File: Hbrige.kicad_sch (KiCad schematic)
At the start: 15 parts, among them U4 CSD88537ND, U5 CSD88537ND

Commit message: reintroduction des mosfet (au lieu des demi-ponts en H), début routage
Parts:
- removed U4, U5: CSD88537ND, CSD88537ND:SOIC127P599X175-8N, symbol CSD88537ND:CSD88537ND
- added J4: Conn_01x02, KF301-5.0-2P:KF301-5.0-2P, symbol Connector_Generic:Conn_01x02
- added U4, U5, U6, U7: ~, TPH1R403NL:TPH1R403NL, symbol DRV8701:TPH1R403NL
- C10, C8: value 0.1u -> 100n; footprint Capacitor_SMD:C_0603_1608Metric_Pad1.08x0.95mm_HandSolder -> Capacitor_SMD:C_0402_1005Metric
- C6, C7, C9: footprint Capacitor_SMD:C_0603_1608Metric_Pad1.08x0.95mm_HandSolder -> Capacitor_SMD:C_0402_1005Metric
- R10, R11, R6, R7, R8, R9: footprint Resistor_SMD:R_0402_1005Metric_Pad0.72x0.64mm_HandSolder -> Resistor_SMD:R_0402_1005Metric
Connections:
- net SH1: now also U3.18 (SH1), J4.2 (Pin_2), U6.5 (D), U6.6 (D), U6.7 (D), U6.8 (D), U6.9 (D), U7.1 (S), U7.2 (S), U7.3 (S)
- net SH2: now also J4.1 (Pin_1), U4.1 (S), U4.2 (S), U4.3 (S), U5.5 (D), U5.6 (D), U5.7 (D), U5.8 (D), U5.9 (D)
- net VDC: now also U4.5 (D), U4.6 (D), U4.7 (D), U4.8 (D), U4.9 (D), U7.5 (D), U7.6 (D), U7.7 (D), U7.8 (D), U7.9 (D)
- net at U3.17 (GH1): now also U7.4 (G)
- net at U3.19 (GL1): now also U6.4 (G)
- net SP: now reaches R11.1, U3.21 (SP)
- net SP: now also U5.1 (S), U5.2 (S), U5.3 (S), U6.1 (S), U6.2 (S), U6.3 (S)
- net at U3.22 (GL2): now also U5.4 (G)
- net at U3.24 (GH2): now also U4.4 (G)

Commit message: maj PCB
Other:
- moved on the sheet: J4
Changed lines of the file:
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@@
 	(wire
 		(pts
-			(xy 217.17 83.82) (xy 217.17 102.87)
+			(xy 217.17 87.63) (xy 217.17 102.87)
 		)
 		(stroke
@@
 	(wire
 		(pts
-			(xy 217.17 81.28) (xy 217.17 69.85)
+			(xy 217.17 85.09) (xy 217.17 69.85)
 		)
 		(stroke
@@
 	(symbol
 		(lib_id "Connector_Generic:Conn_01x02")
-		(at 222.25 81.28 0)
+		(at 222.25 85.09 0)
 		(unit 1)
 		(exclude_from_sim no)
@@
 		(dnp no)
 		(property "Reference" "J4"
-			(at 221.996 89.408 90)
+			(at 221.996 93.218 90)
 			(effects
 				(font
@@
 		)
 		(property "Value" "Conn_01x02"
-			(at 224.79 87.884 90)
+			(at 224.79 91.694 90)
 			(effects
 				(font
@@
 		)
 		(property "Footprint" "KF301-5.0-2P:KF301-5.0-2P"
-			(at 222.25 81.28 0)
+			(at 222.25 85.09 0)
 			(effects
 				(font
@@
 		)
 		(property "Datasheet" "~"
-			(at 222.25 81.28 0)
+			(at 222.25 85.09 0)
 			(effects
 				(font
@@
 		)
 		(property "Description" "Generic connector, single row, 01x02, script generated (kicad-library-utils/schlib/autogen/connector/)"
-			(at 222.25 81.28 0)
-			(effects
-				(font
+			(at 222.25 85.09 0)
+			(effects
+				(font

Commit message: finalisation PCB
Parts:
- removed C6: 1u, Capacitor_SMD:C_0402_1005Metric, symbol Device:C
- removed R10: 3.3k, Resistor_SMD:R_0402_1005Metric, symbol Device:R
- removed R11: 50m, Resistor_SMD:R_0402_1005Metric, symbol Device:R
- removed R6, R7: 10k, Resistor_SMD:R_0402_1005Metric, symbol Device:R
- removed R8: 33k, Resistor_SMD:R_0402_1005Metric, symbol Device:R
- removed R9: 2k, Resistor_SMD:R_0402_1005Metric, symbol Device:R
- added C12: 1u, Capacitor_SMD:C_0402_1005Metric, symbol Device:C
- renumbered C7 to C11, C8 to C13, C9 to C14, C10 to C15, C11 to C16, U3 to U5, U4 to U6, U5 to U7, U6 to U8, U7 to U9
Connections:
- net GND: now also U5.21 (SP), C12.2
- net SH2: now also U5.22 (GL2), U7.4 (G)
- net at U5.7 (AVDD): now also U5.12 (IDRIVE), U5.6 (VREF), C12.1
- net SNSOUT: no longer names the net of U5.10 (SNSOUT)
- net SO: no longer names the net of U5.11 (SO)
- net SP renamed jonctionSS
- net jonctionSS: no longer U5.21 (SP)
- net nFAULT: no longer names the net of U5.9 (nFAULT)
- no-connect marks 0 -> 3
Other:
- moved on the sheet: C11, U6, U7, U9

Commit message: final push
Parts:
- removed C16: 47u, Capacitor:Wurth-47u-63V, symbol Device:C_Polarized
- added C16: 10u, Capacitor_SMD:C_0805_2012Metric, symbol Device:C
- renumbered U8 to U7, U7 to U8
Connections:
- net GND: now also U7.1 (S), U7.2 (S), U7.3 (S), U9.1 (S), U9.2 (S), U9.3 (S), C16.1
- net SH1: now also J4.1 (Pin_1), U8.1 (S), U8.2 (S), U8.3 (S), U9.5 (D), U9.6 (D), U9.7 (D), U9.8 (D), U9.9 (D); no longer J4.2 (Pin_2), U7.5 (D), U7.6 (D), U7.7 (D), U7.8 (D), U7.9 (D), U9.1 (S), U9.2 (S), U9.3 (S)
- net SH2: now also J4.2 (Pin_2), U7.5 (D), U7.6 (D), U7.7 (D), U7.8 (D), U7.9 (D); no longer J4.1 (Pin_1), U5.22 (GL2), U8.4 (G), U8.5 (D), U8.6 (D), U8.7 (D), U8.8 (D), U8.9 (D)
- net VDC: now also U8.5 (D), U8.6 (D), U8.7 (D), U8.8 (D), U8.9 (D), C16.2; no longer U9.5 (D), U9.6 (D), U9.7 (D), U9.8 (D), U9.9 (D)
- net GH2: now reaches U5.24 (GH2), U6.4 (G)
- net GH1: now reaches U5.17 (GH1)
- net GH1: now also U8.4 (G); no longer U9.4 (G)
- net GL1: now reaches U5.19 (GL1)
- net GL1: now also U9.4 (G); no longer U7.4 (G)
- removed net jonctionSS: U7.1 (S), U7.2 (S), U7.3 (S), U8.1 (S), U8.2 (S), U8.3 (S)
- new net GL2: U5.22 (GL2), U7.4 (G)
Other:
- moved on the sheet: C11, C12, C13, C14, C15, J4, U5, U6, U7, U8, U9

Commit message: modif footprints des condo de puissance
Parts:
- C11, C12, C14: footprint Capacitor_SMD:C_0402_1005Metric -> Capacitor_SMD:C_0805_2012Metric
- C13, C15: footprint Capacitor_SMD:C_0402_1005Metric -> Capacitor_SMD:C_0603_1608Metric
- C16: footprint Capacitor_SMD:C_0805_2012Metric -> Capacitor_SMD:C_1206_3216Metric
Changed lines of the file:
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@@
 			)
 		)
-		(property "Footprint" "Capacitor_SMD:C_0805_2012Metric"
+		(property "Footprint" "Capacitor_SMD:C_1206_3216Metric"
 			(at 127.3048 54.61 0)
 			(effects
@@
 			)
 		)
-		(property "Footprint" "Capacitor_SMD:C_0402_1005Metric"
+		(property "Footprint" "Capacitor_SMD:C_0805_2012Metric"
 			(at 87.9348 50.8 0)
 			(effects
@@
 			)
 		)
-		(property "Footprint" "Capacitor_SMD:C_0402_1005Metric"
+		(property "Footprint" "Capacitor_SMD:C_0805_2012Metric"
 			(at 54.61 77.1652 0)
 			(effects
@@
 			)
 		)
-		(property "Footprint" "Capacitor_SMD:C_0402_1005Metric"
+		(property "Footprint" "Capacitor_SMD:C_0603_1608Metric"
 			(at 95.5548 44.45 0)
 			(effects
@@
 			)
 		)
-		(property "Footprint" "Capacitor_SMD:C_0402_1005Metric"
+		(property "Footprint" "Capacitor_SMD:C_0603_1608Metric"
 			(at 114.6048 54.61 0)
 			(effects
@@
 			)
 		)
-		(property "Footprint" "Capacitor_SMD:C_0402_1005Metric"
+		(property "Footprint" "Capacitor_SMD:C_0805_2012Metric"
 			(at 100.33 55.5752 0)
 			(effects

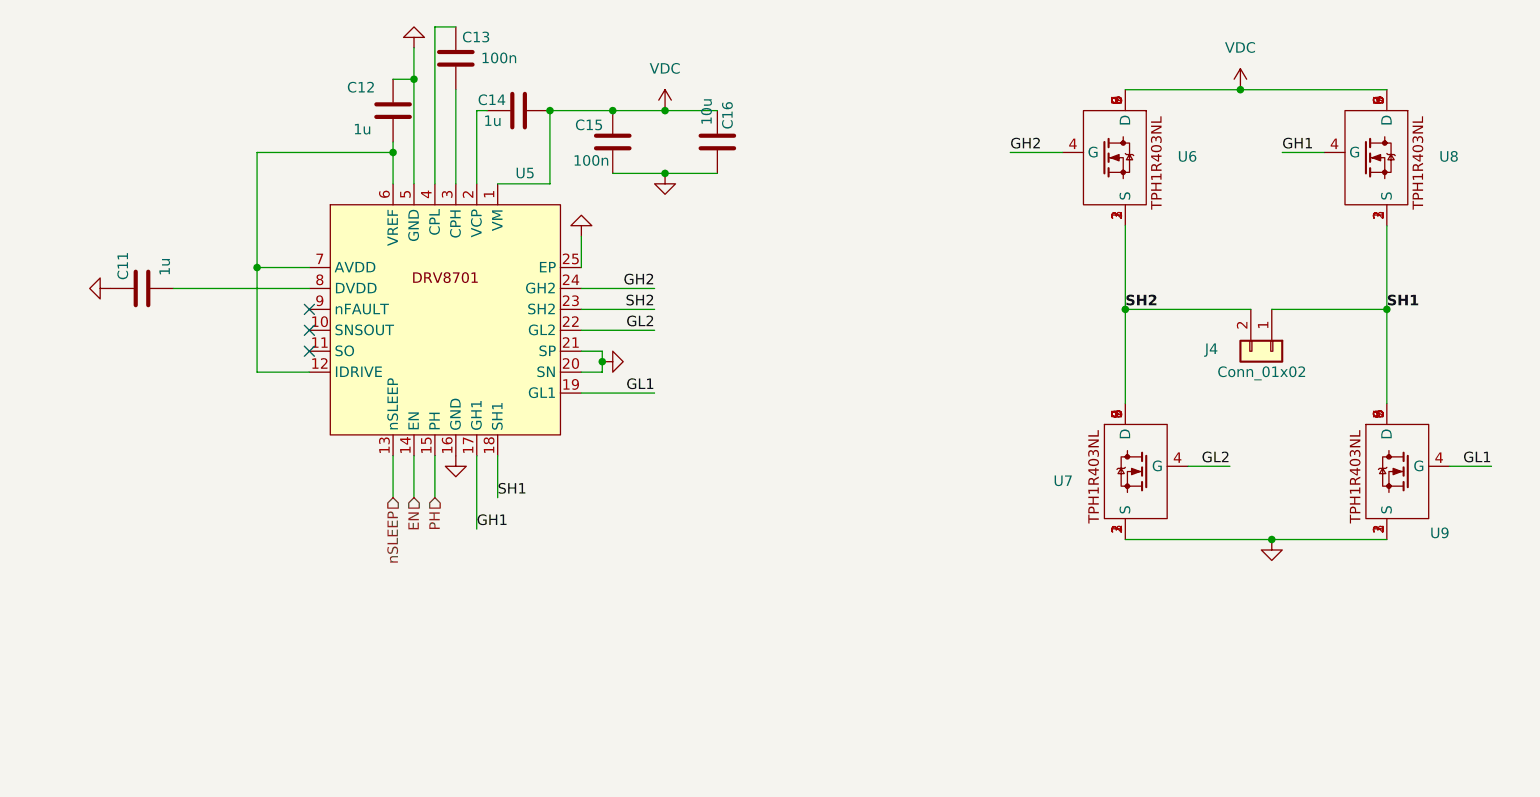
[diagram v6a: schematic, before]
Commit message: V2 Driver-- avec control de courant
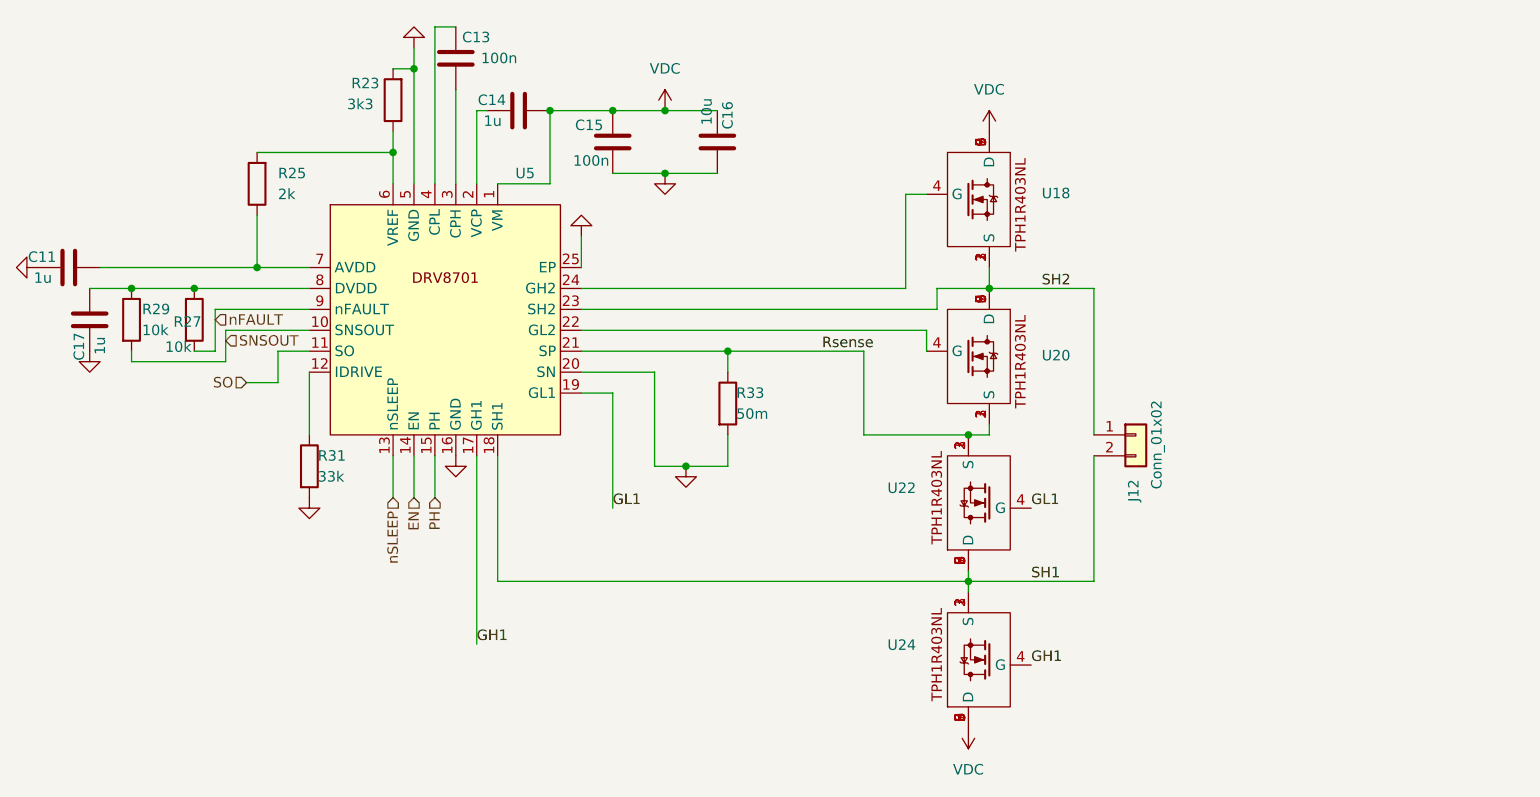
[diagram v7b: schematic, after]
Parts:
- removed C12: 1u, Capacitor_SMD:C_0805_2012Metric, symbol Device:C
- removed J4: Conn_01x02, KF301-5.0-2P:KF301-5.0-2P, symbol Connector_Generic:Conn_01x02
- removed U6, U7, U8, U9: ~, TPH1R403NL:TPH1R403NL, symbol DRV8701:TPH1R403NL
- added C17: 1u, Capacitor_SMD:C_0603_1608Metric, symbol Device:C
- added J12: Conn_01x02, KF301-5.0-2P:KF301-5.0-2P, symbol Connector_Generic:Conn_01x02
- added R23: 3k3, Resistor_SMD:R_0402_1005Metric, symbol Device:R
- added R25: 2k, Resistor_SMD:R_0402_1005Metric, symbol Device:R
- added R27, R29: 10k, Resistor_SMD:R_0402_1005Metric, symbol Device:R
- added R31: 33k, Resistor_SMD:R_0402_1005Metric, symbol Device:R
- added R33: 50m, Resistor_SMD:R_2512_6332Metric, symbol Device:R
- added U18, U20, U22, U24: ~, TPH1R403NL:TPH1R403NL, symbol DRV8701:TPH1R403NL
- C11: footprint Capacitor_SMD:C_0805_2012Metric -> Capacitor_SMD:C_0603_1608Metric
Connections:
- net GH1: now also U24.4 (G)
- net GL1: now also U22.4 (G)
- net GND: now also C17.2, R23.2, R31.2, R33.2; no longer U5.21 (SP)
- net SH1: now also J12.2 (Pin_2), U22.5 (D), U22.6 (D), U22.7 (D), U22.8 (D), U22.9 (D), U24.1 (S), U24.2 (S), U24.3 (S)
- net SH2: now also J12.1 (Pin_1), U18.1 (S), U18.2 (S), U18.3 (S), U20.5 (D), U20.6 (D), U20.7 (D), U20.8 (D), U20.9 (D)
- net VDC: now also U18.5 (D), U18.6 (D), U18.7 (D), U18.8 (D), U18.9 (D), U24.5 (D), U24.6 (D), U24.7 (D), U24.8 (D), U24.9 (D)
- net SNSOUT: now reaches U5.10 (SNSOUT)
- net SNSOUT: now also R29.2
- net SO: now reaches U5.11 (SO)
- net at C11.1: now also U5.7 (AVDD), R25.1; no longer U5.8 (DVDD)
- net nFAULT: now reaches U5.9 (nFAULT)
- net nFAULT: now also R27.2
- net GH2: no longer names the net of U5.24 (GH2)
- net GH2: now also U18.4 (G)
- net GL2: no longer names the net of U5.22 (GL2)
- net GL2: now also U20.4 (G)
- new net: R23.1, R25.2, U5.6 (VREF)
- new net: R31.1, U5.12 (IDRIVE)
- new net: C17.1, R27.1, R29.1, U5.8 (DVDD)
- new net Rsense: R33.1, U20.1 (S), U20.2 (S), U20.3 (S), U22.1 (S), U22.2 (S), U22.3 (S), U5.21 (SP)
- no-connect marks 3 -> 0

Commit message: final push
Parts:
- U5: value ~ -> DRV8701
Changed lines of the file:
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@@
 			)
 		)
-		(property "Value" "~"
+		(property "Value" "DRV8701"
 			(at 103.7433 64.77 0)
 			(effects
